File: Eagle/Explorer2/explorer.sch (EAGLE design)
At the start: 10 parts

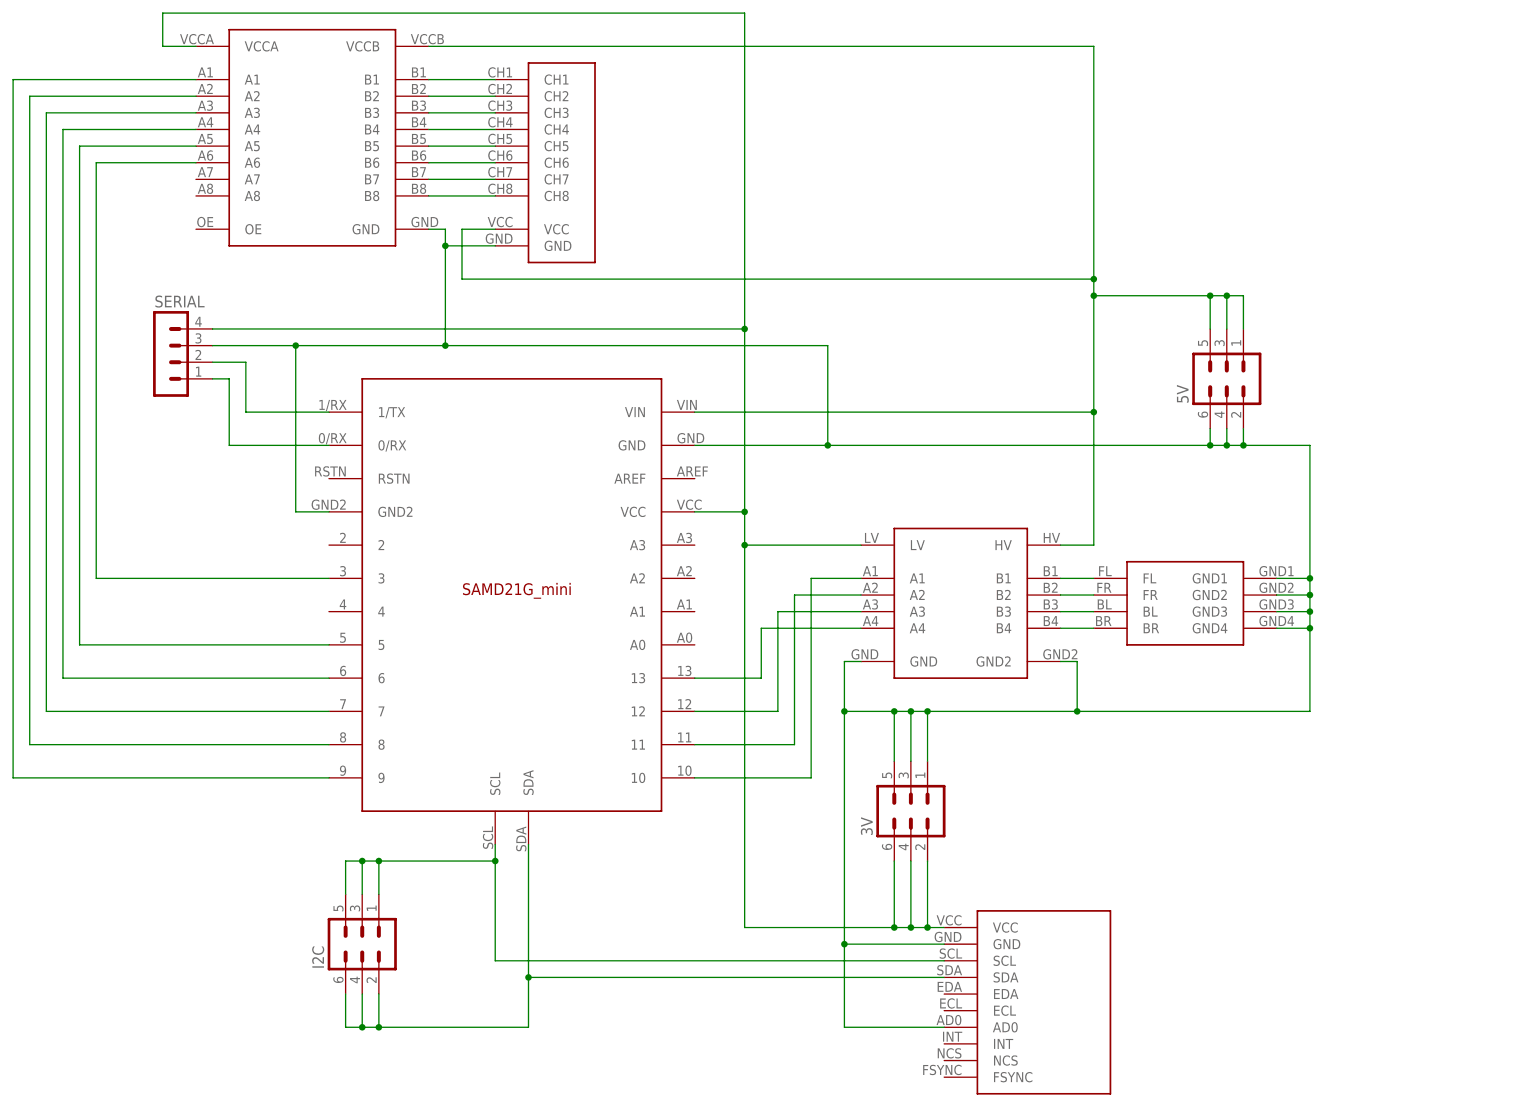
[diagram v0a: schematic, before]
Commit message: Redesigned Explorer2 board to use two copper layers. Cleaned up and tested Explorer2 code, ready for test.
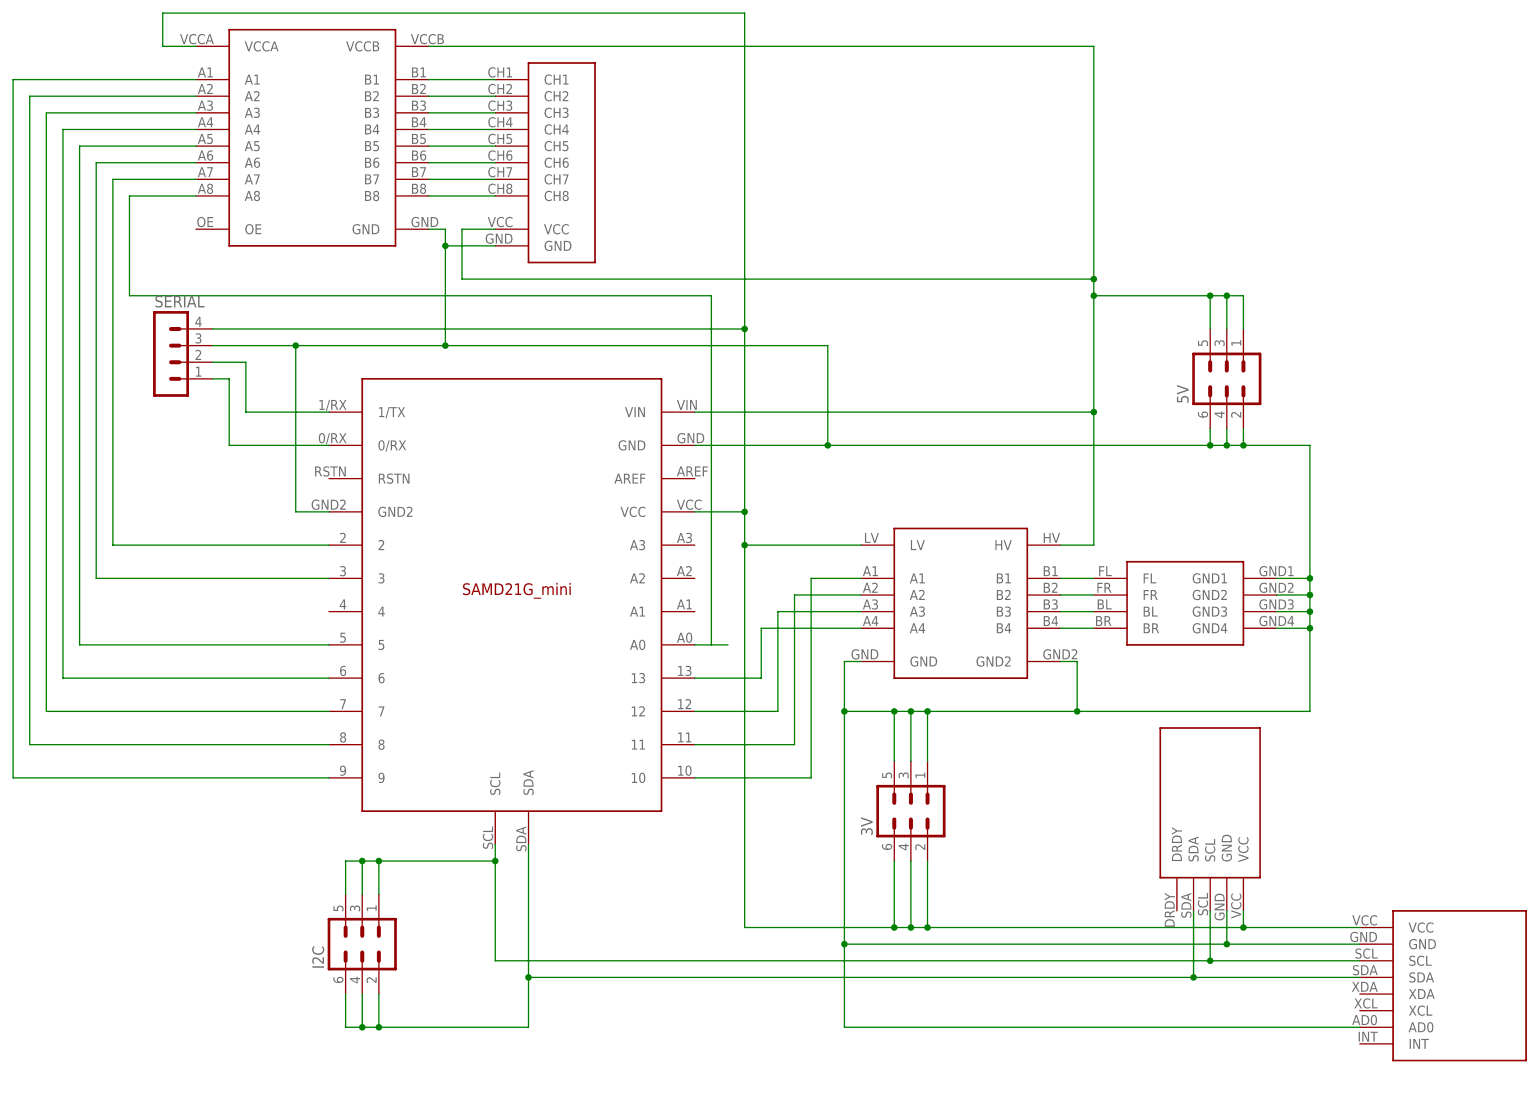
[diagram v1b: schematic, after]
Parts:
- added U$5: LEVELSHIFT_4CH, quadcopter_comp:LEVELSHIFT_4CH
- U$2: value MPU9250 -> MPU6050; device quadcopter_comp:MPU9250 -> quadcopter_comp:MPU6050
- U$7: value LEVELSHIFT_4CH -> HMC5883L; device quadcopter_comp:LEVELSHIFT_4CH -> quadcopter_comp:HMC5883L
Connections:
- new net N$19: U$3.2, U$4.A7
- new net N$25: U$3.A0, U$4.A8
- net 3V: now also U$5.LV, U$7.VCC; no longer U$7.LV
- net 5V: now also U$5.HV; no longer U$7.HV
- net GND: now also U$5.GND, U$5.GND2; no longer U$7.GND2
- net N$1: now also U$5.B4; no longer U$7.B4
- net N$10: now also U$5.A4; no longer U$7.A4
- net N$2: now also U$5.B3; no longer U$7.B3
- net N$26: now also U$7.SCL
- net N$28: now also U$7.SDA
- net N$3: now also U$5.B2; no longer U$7.B2
- net N$4: now also U$5.B1; no longer U$7.B1
- net N$7: now also U$5.A1; no longer U$7.A1
- net N$8: now also U$5.A2; no longer U$7.A2
- net N$9: now also U$5.A3; no longer U$7.A3

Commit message: Replaced all sensor breakout boards with one gy-86 board. Started on pids for altitude hold.
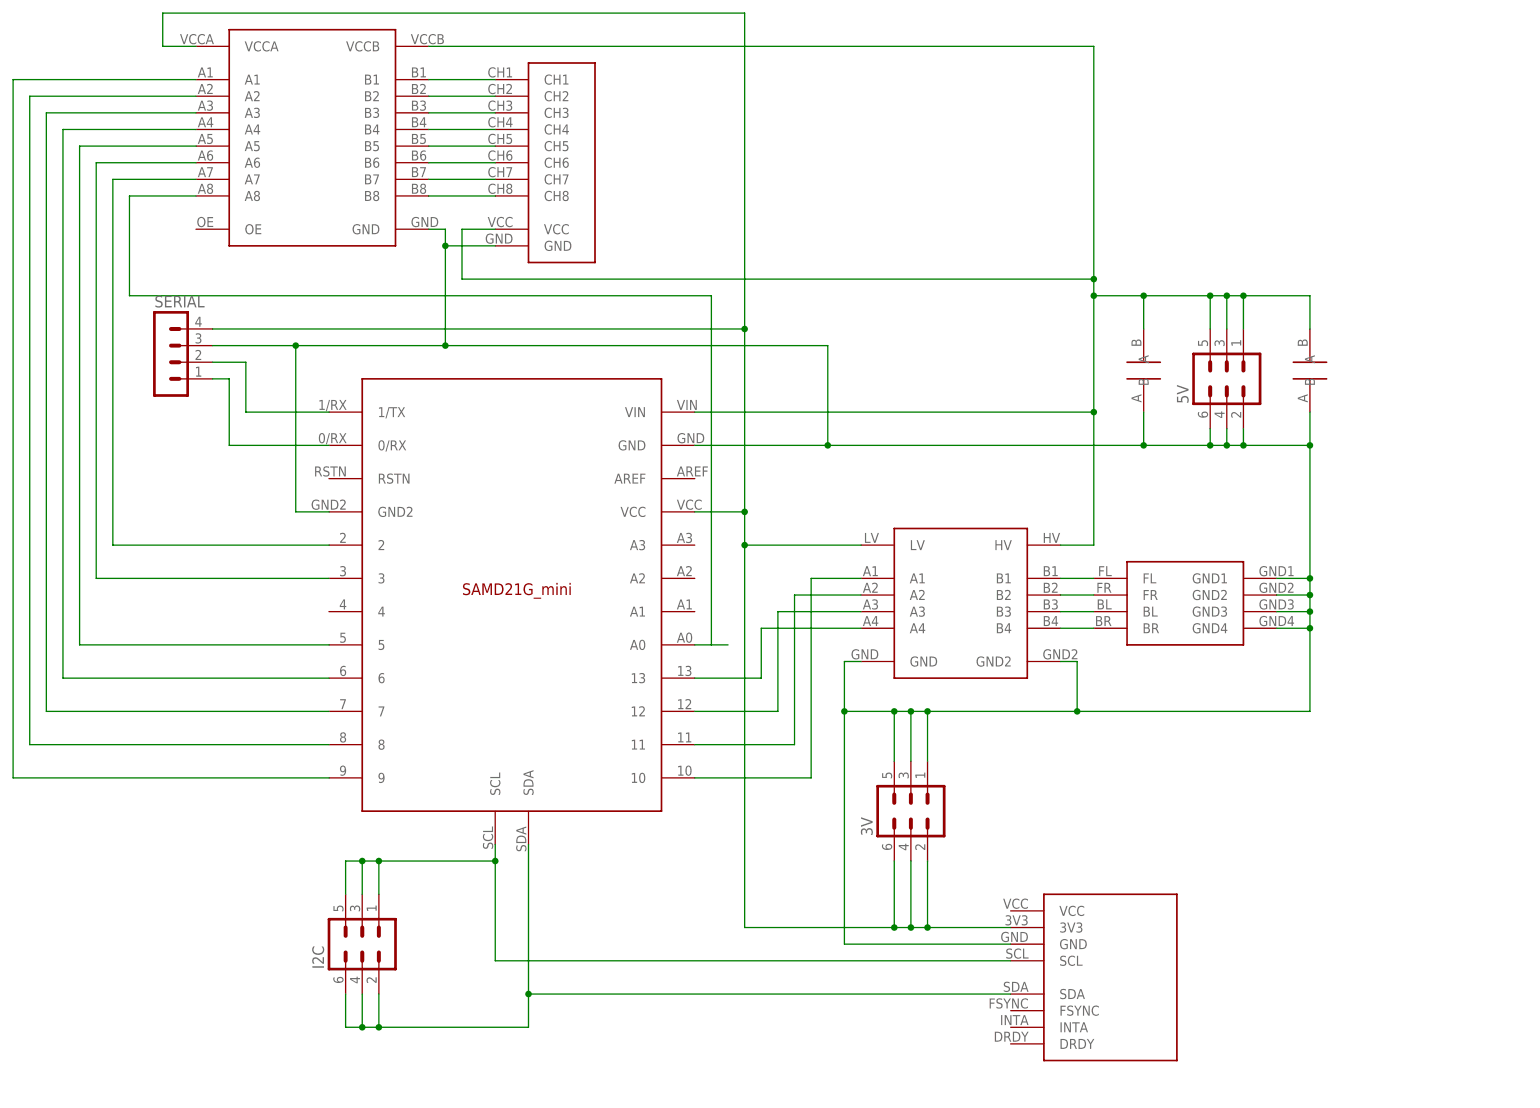
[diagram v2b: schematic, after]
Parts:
- added U$8: GY-86, quadcopter_comp:GY-86
- U$2: value MPU6050 -> CAP; device quadcopter_comp:MPU6050 -> quadcopter_comp:CAP
- U$7: value HMC5883L -> CAP; device quadcopter_comp:HMC5883L -> quadcopter_comp:CAP
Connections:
- net 3V: now also U$8.3V3; no longer U$2.VCC, U$7.VCC
- net 5V: now also U$2.B, U$7.B
- net GND: now also U$2.A, U$7.A, U$8.GND; no longer U$2.AD0, U$2.GND, U$7.GND
- net N$26: now also U$8.SCL; no longer U$2.SCL, U$7.SCL
- net N$28: now also U$8.SDA; no longer U$2.SDA, U$7.SDA
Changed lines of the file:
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@@
 <part name="5V" library="con-lstb" deviceset="MA03-2" device=""/>
 <part name="SERIAL" library="con-lstb" deviceset="MA04-1" device=""/>
-<part name="U$2" library="quadcopter_comp" deviceset="MPU6050" device=""/>
 <part name="U$5" library="quadcopter_comp" deviceset="LEVELSHIFT_4CH" device=""/>
-<part name="U$7" library="quadcopter_comp" deviceset="HMC5883L" device=""/>
+<part name="U$8" library="quadcopter_comp" deviceset="GY-86" device=""/>
+<part name="U$2" library="quadcopter_comp" deviceset="CAP" device=""/>
+<part name="U$7" library="quadcopter_comp" deviceset="CAP" device=""/>
 </parts>
 <sheets>
@@
 <instance part="5V" gate="1" x="109.22" y="33.02" rot="R90"/>
 <instance part="SERIAL" gate="1" x="-53.34" y="38.1"/>
-<instance part="U$2" gate="G$1" x="144.78" y="-60.96"/>
 <instance part="U$5" gate="G$1" x="68.58" y="-2.54"/>
-<instance part="U$7" gate="G$1" x="106.68" y="-30.48" rot="R270"/>
+<instance part="U$8" gate="G$1" x="91.44" y="-58.42"/>
+<instance part="U$2" gate="G$1" x="96.52" y="35.56" rot="R90"/>
+<instance part="U$7" gate="G$1" x="121.92" y="35.56" rot="R90"/>
 </instances>
 <busses>
@@
 <junction x="121.92" y="-2.54"/>
 <junction x="121.92" y="-5.08"/>
-<wire x1="129.54" y1="-53.34" x2="109.22" y2="-53.34" width="0.1524" layer="91"/>
-<wire x1="109.22" y1="-53.34" x2="50.8" y2="-53.34" width="0.1524" layer="91"/>
+<wire x1="76.2" y1="-53.34" x2="50.8" y2="-53.34" width="0.1524" layer="91"/>
 <wire x1="50.8" y1="-53.34" x2="50.8" y2="-17.78" width="0.1524" layer="91"/>
 <junction x="50.8" y="-17.78"/>
-<wire x1="129.54" y1="-66.04" x2="50.8" y2="-66.04" width="0.1524" layer="91"/>
-<wire x1="50.8" y1="-66.04" x2="50.8" y2="-53.34" width="0.1524" layer="91"/>
-<junction x="50.8" y="-53.34"/>
 <pinref part="5V" gate="1" pin="6"/>
 <wire x1="106.68" y1="25.4" x2="106.68" y2="22.86" width="0.1524" layer="91"/>
@@
 <junction x="60.96" y="-17.78"/>
 <junction x="58.42" y="-17.78"/>
-<wire x1="48.26" y1="22.86" x2="106.68" y2="22.86" width="0.1524" layer="91"/>
+<wire x1="48.26" y1="22.86" x2="96.52" y2="22.86" width="0.1524" layer="91"/>
+<wire x1="96.52" y1="22.86" x2="106.68" y2="22.86" width="0.1524" layer="91"/>
 <wire x1="-10.16" y1="53.34" x2="-10.16" y2="38.1" width="0.1524" layer="91"/>
 <pinref part="U$3" gate="G$1" pin="GND2"/>
@@
 <junction x="48.26" y="22.86"/>
 <junction x="106.68" y="22.86"/>
-<pinref part="U$2" gate="G$1" pin="GND"/>
-<pinref part="U$2" gate="G$1" pin="AD0"/>
 <pinref part="U$5" gate="G$1" pin="GND2"/>
 <pinref part="U$5" gate="G$1" pin="GND"/>
-<pinref part="U$7" gate="G$1" pin="GND"/>
-<wire x1="109.22" y1="-48.26" x2="109.22" y2="-53.34" width="0.1524" layer="91"/>
-<junction x="109.22" y="-53.34"/>
+<pinref part="U$8" gate="G$1" pin="GND"/>
+<pinref part="U$2" gate="G$1" pin="A"/>
+<wire x1="96.52" y1="27.94" x2="96.52" y2="22.86" width="0.1524" layer="91"/>
+<pinref part="U$7" gate="G$1" pin="A"/>
+<wire x1="121.92" y1="27.94" x2="121.92" y2="22.86" width="0.1524" layer="91"/>
+<junction x="96.52" y="22.86"/>
+<junction x="121.92" y="22.86"/>
 </segment>
 </net>
@@
 <pinref part="5V" gate="1" pin="3"/>
 <wire x1="109.22" y1="45.72" x2="106.68" y2="45.72" width="0.1524" layer="91"/>
-<wire x1="106.68" y1="45.72" x2="88.9" y2="45.72" width="0.1524" layer="91"/>
+<wire x1="106.68" y1="45.72" x2="96.52" y2="45.72" width="0.1524" layer="91"/>
+<wire x1="96.52" y1="45.72" x2="88.9" y2="45.72" width="0.1524" layer="91"/>
 <wire x1="109.22" y1="40.64" x2="109.22" y2="45.72" width="0.1524" layer="91"/>
 <pinref part="5V" gate="1" pin="5"/>
@@
 <junction x="109.22" y="45.72"/>
 <pinref part="U$5" gate="G$1" pin="HV"/>
+<pinref part="U$2" gate="G$1" pin="B"/>
+<wire x1="96.52" y1="40.64" x2="96.52" y2="45.72" width="0.1524" layer="91"/>
+<pinref part="U$7" gate="G$1" pin="B"/>
+<wire x1="111.76" y1="45.72" x2="121.92" y2="45.72" width="0.1524" layer="91"/>
+<wire x1="121.92" y1="45.72" x2="121.92" y2="40.64" width="0.1524" layer="91"/>
+<junction x="96.52" y="45.72"/>
+<junction x="111.76" y="45.72"/>
 </segment>
 </net>
@@
 <wire x1="58.42" y1="-50.8" x2="60.96" y2="-50.8" width="0.1524" layer="91"/>
 <wire x1="60.96" y1="-50.8" x2="63.5" y2="-50.8" width="0.1524" layer="91"/>
-<wire x1="63.5" y1="-50.8" x2="111.76" y2="-50.8" width="0.1524" layer="91"/>
-<wire x1="111.76" y1="-50.8" x2="129.54" y2="-50.8" width="0.1524" layer="91"/>
+<wire x1="63.5" y1="-50.8" x2="76.2" y2="-50.8" width="0.1524" layer="91"/>
 <wire x1="58.42" y1="-40.64" x2="58.42" y2="-50.8" width="0.1524" layer="91"/>
 <pinref part="3V" gate="1" pin="2"/>
@@
 <wire x1="-45.72" y1="40.64" x2="35.56" y2="40.64" width="0.1524" layer="91"/>
 <junction x="35.56" y="40.64"/>
-<pinref part="U$2" gate="G$1" pin="VCC"/>
 <pinref part="U$5" gate="G$1" pin="LV"/>
-<pinref part="U$7" gate="G$1" pin="VCC"/>
-<wire x1="111.76" y1="-48.26" x2="111.76" y2="-50.8" width="0.1524" layer="91"/>
-<junction x="111.76" y="-50.8"/>
+<pinref part="U$8" gate="G$1" pin="3V3"/>
 </segment>
 </net>
@@
 <segment>
 <pinref part="U$3" gate="G$1" pin="SCL"/>
-<wire x1="129.54" y1="-55.88" x2="106.68" y2="-55.88" width="0.1524" layer="91"/>
-<wire x1="106.68" y1="-55.88" x2="-2.54" y2="-55.88" width="0.1524" layer="91"/>
+<wire x1="76.2" y1="-55.88" x2="-2.54" y2="-55.88" width="0.1524" layer="91"/>
 <wire x1="-2.54" y1="-55.88" x2="-2.54" y2="-40.64" width="0.1524" layer="91"/>
 <pinref part="I2C" gate="1" pin="5"/>
@@
 <junction x="-20.32" y="-40.64"/>
 <junction x="-22.86" y="-40.64"/>
-<pinref part="U$2" gate="G$1" pin="SCL"/>
-<pinref part="U$7" gate="G$1" pin="SCL"/>
-<wire x1="106.68" y1="-48.26" x2="106.68" y2="-55.88" width="0.1524" layer="91"/>
-<junction x="106.68" y="-55.88"/>
+<pinref part="U$8" gate="G$1" pin="SCL"/>
 </segment>
 </net>
@@
 <segment>
 <pinref part="U$3" gate="G$1" pin="SDA"/>
-<wire x1="129.54" y1="-58.42" x2="104.14" y2="-58.42" width="0.1524" layer="91"/>
-<wire x1="104.14" y1="-58.42" x2="2.54" y2="-58.42" width="0.1524" layer="91"/>
-<wire x1="2.54" y1="-58.42" x2="2.54" y2="-38.1" width="0.1524" layer="91"/>
+<wire x1="2.54" y1="-66.04" x2="2.54" y2="-60.96" width="0.1524" layer="91"/>
 <pinref part="I2C" gate="1" pin="6"/>
+<wire x1="2.54" y1="-60.96" x2="2.54" y2="-38.1" width="0.1524" layer="91"/>
 <wire x1="-25.4" y1="-60.96" x2="-25.4" y2="-66.04" width="0.1524" layer="91"/>
 <wire x1="-25.4" y1="-66.04" x2="-22.86" y2="-66.04" width="0.1524" layer="91"/>
 <wire x1="-22.86" y1="-66.04" x2="-20.32" y2="-66.04" width="0.1524" layer="91"/>
 <wire x1="-20.32" y1="-66.04" x2="2.54" y2="-66.04" width="0.1524" layer="91"/>
-<wire x1="2.54" y1="-66.04" x2="2.54" y2="-58.42" width="0.1524" layer="91"/>
 <pinref part="I2C" gate="1" pin="4"/>
 <wire x1="-22.86" y1="-60.96" x2="-22.86" y2="-66.04" width="0.1524" layer="91"/>
 <pinref part="I2C" gate="1" pin="2"/>
 <wire x1="-20.32" y1="-60.96" x2="-20.32" y2="-66.04" width="0.1524" layer="91"/>
-<junction x="2.54" y="-58.42"/>
 <junction x="-22.86" y="-66.04"/>
 <junction x="-20.32" y="-66.04"/>
-<pinref part="U$2" gate="G$1" pin="SDA"/>
-<pinref part="U$7" gate="G$1" pin="SDA"/>
-<wire x1="104.14" y1="-48.26" x2="104.14" y2="-58.42" width="0.1524" layer="91"/>
-<junction x="104.14" y="-58.42"/>
-</segment>
-</net>
+<pinref part="U$8" gate="G$1" pin="SDA"/>
+<wire x1="76.2" y1="-60.96" x2="2.54" y2="-60.96" width="0.1524" layer="91"/>
+<junction x="2.54" y="-60.96"/>
+</segment>
+</net>
